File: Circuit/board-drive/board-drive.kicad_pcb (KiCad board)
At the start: 2 copper layers, 164.4 x 98.3 mm, 32 parts, among them M3 MountingHole_3.2mm_M3, P1 XT30, P10 XT60, P2 XT30, P3 XT30, P4 XT30, P5 XT30, P6 XT30, P7 XT30, P8 XT30, P9 XT60, U1 Pololu_Maestro12, U10 PowerDist_WiretoBoard, U11 PowerDist_WiretoBoard, U16 PowerDist_WiretoBoard, U17 PowerDist_WiretoBoard, U18 PowerDist_WiretoBoard, U19 PowerDist_WiretoBoard, U2 Si8660BA-B-IS1, U3 Si8660BA-B-IS1, U8 PowerDist_WiretoBoard, U9 PowerDist_WiretoBoard

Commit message: edited pcb
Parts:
- moved U1 27.8 mm to (52.9, 140.5), turned to 90 degrees
- moved U3 12.4 mm to (78.7, 129.2), turned to 0 degrees
- moved U2 7.31 mm to (65.2, 129.2), turned to 0 degrees
- moved Board Drive 0 6.84 mm to (150.1, 118.6)
- moved Board Drive 1 6.84 mm to (208.6, 119.1)
- moved Board Drive 6 6.84 mm to (208.5, 118.6)
- moved Board Drive 7 6.84 mm to (150.2, 119.1)
- moved Board Drive 2 6.84 mm to (89.9, 118.6)
- moved Board Drive 5 6.84 mm to (89.9, 119.0)
- moved Board Drive 3 6.84 mm to (148.3, 119.0)
- moved Board Drive 4 6.84 mm to (148.3, 118.6)
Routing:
- net GNDA: track 37.7 -> 4.89 mm, vias 2 -> 0
- net /signal0: track 108.7 -> 127.2 mm, vias 1 -> 0
- net /signal1: track 136.2 -> 153.9 mm
- net /signal7: track 24.2 -> 41.6 mm
- net /signal3: track 75.3 -> 90.5 mm, vias 3 -> 1
- net /signal2: track 58.5 -> 44.0 mm, vias 1 -> 0
- net GNDD: track 17.9 -> 4.23 mm
- net /BATTIN_0: track 182.7 -> 174.4 mm
- net /BATTIN_1: track 234.3 -> 241.3 mm
- net /signal8: track 132.6 -> 138.2 mm, vias 0 -> 3
- net /+5v_BEC: track 38.3 -> 43.7 mm
- net /signal6: track 73.5 -> 77.7 mm, vias 0 -> 3
- net /signal9: track 93.8 -> 92.1 mm

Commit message: edited pcb
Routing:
- net /signal2: track 44.0 -> 46.4 mm, vias 0 -> 1
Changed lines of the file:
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@@
   (general
     (links 81)
-    (no_connects 0)
-    (area 43.017657 50.474599 226.07515 197.434901)
+    (no_connects 3)
+    (area 43.017657 50.474599 226.07515 152.2934)
     (thickness 1.6)
     (drawings 38)
-    (tracks 269)
+    (tracks 270)
     (zones 0)
     (modules 32)
@@
   )
   (setup
-    (last_trace_width 2.3622)
+    (last_trace_width 0.254)
     (user_trace_width 0.254)
     (user_trace_width 0.381)
@@
   (segment (start 63.326651 132.163471) (end 63.326651 131.856737) (width 0.1524) (layer B.Cu) (net 17))
   (segment (start 63.326651 131.856737) (end 63.326651 132.331737) (width 0.254) (layer B.Cu) (net 17))
-  (segment (start 67.1322 128.4478) (end 65.6844 129.8956) (width 0.254) (layer F.Cu) (net 18))
+  (segment (start 65.7606 129.9464) (end 64.596651 131.110349) (width 0.254) (layer B.Cu) (net 18))
+  (segment (start 64.596651 131.110349) (end 64.596651 131.856737) (width 0.254) (layer B.Cu) (net 18))
+  (via (at 65.7606 129.9464) (size 0.6) (drill 0.381) (layers F.Cu B.Cu) (net 18))
+  (segment (start 67.2084 128.4986) (end 65.7606 129.9464) (width 0.254) (layer F.Cu) (net 18))
   (segment (start 84.9122 128.4986) (end 67.2084 128.4986) (width 0.254) (layer F.Cu) (net 18))
   (segment (start 87.7316 125.6792) (end 84.9122 128.4986) (width 0.254) (layer F.Cu) (net 18))
@@
   (segment (start 72.507965 131.856737) (end 72.883975 132.232747) (width 0.1524) (layer B.Cu) (net 22))
   (segment (start 69.676651 131.856737) (end 72.507965 131.856737) (width 0.1524) (layer B.Cu) (net 22))
-  (segment (start 58.024975 128.879947) (end 58.101175 128.956147) (width 0.381) (layer B.Cu) (net 23))
-  (segment (start 58.024975 128.879947) (end 58.024975 128.549747) (width 0.254) (layer B.Cu) (net 23))
   (segment (start 69.676651 124.518071) (end 70.978975 123.215747) (width 0.254) (layer B.Cu) (net 23))
   (segment (start 69.676651 126.468737) (end 69.676651 124.518071) (width 0.254) (layer B.Cu) (net 23))
@@
   )
   (zone (net 22) (net_name GNDA) (layer B.Cu) (hatch edge 0.508)
-    (connect_pads (clearance 0.508))
+    (connect_pads yes (clearance 0.508))
     (min_thickness 0.254)
     (fill yes (arc_segments 16) (thermal_gap 0.508) (thermal_bridge_width 0.508))
     (polygon
       (pts
-        (xy 50.9524 130.302) (xy 50.927 130.5052) (xy 50.927 149.606) (xy 214.0458 149.4536) (xy 213.7918 109.8296)
-        (xy 89.8906 110.1598) (xy 89.6366 131.1656) (xy 50.927 130.429)
+        (xy 52.0446 130.556) (xy 51.054 130.556) (xy 51.054 149.86) (xy 214.0458 149.4536) (xy 213.7918 109.8296)
+        (xy 89.8906 110.1598) (xy 89.8906 130.6322) (xy 53.0352 130.556)
       )
     )

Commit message: edited pcb
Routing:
- net /signal0: track 127.2 -> 126.8 mm, vias 0 -> 2
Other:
- board size 164.4 x 98.3 mm -> 164.3 x 98.3 mm
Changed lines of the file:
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@@
     (thickness 1.6)
     (drawings 38)
-    (tracks 270)
+    (tracks 274)
     (zones 0)
     (modules 32)
@@
     (effects (font (size 1.5 1.5) (thickness 0.3)))
   )
-  (gr_line (start 50.0126 51.8414) (end 50 150) (angle 90) (layer Edge.Cuts) (width 0.15))
+  (gr_line (start 50.038 51.8414) (end 50.038 150.114) (angle 90) (layer Edge.Cuts) (width 0.15))
   (gr_line (start 50.038 150.114) (end 214.376 150.114) (angle 90) (layer Edge.Cuts) (width 0.15))
   (gr_line (start 214.3506 51.8414) (end 214.376 150.114) (angle 90) (layer Edge.Cuts) (width 0.15))
-  (gr_line (start 50.0126 51.8414) (end 214.3506 51.8414) (angle 90) (layer Edge.Cuts) (width 0.15))
+  (gr_line (start 50.038 51.8414) (end 214.3506 51.8414) (angle 90) (layer Edge.Cuts) (width 0.15))
   (segment (start 71.52639 65.37961) (end 147.72639 65.37961) (width 1.7272) (layer B.Cu) (net 1))
   (segment (start 147.72639 65.37961) (end 152.654 60.452) (width 1.7272) (layer B.Cu) (net 1))
@@
   (segment (start 69.676651 119.156737) (end 74.280975 123.761061) (width 0.254) (layer F.Cu) (net 24))
   (segment (start 60.786651 126.943737) (end 60.786651 126.468737) (width 0.254) (layer B.Cu) (net 24))
+  (segment (start 62.0522 134.118596) (end 62.0522 131.861188) (width 0.254) (layer B.Cu) (net 25))
+  (segment (start 62.0522 131.861188) (end 62.056651 131.856737) (width 0.254) (layer B.Cu) (net 25))
+  (via (at 62.0522 134.118596) (size 0.6) (drill 0.381) (layers F.Cu B.Cu) (net 25))
+  (segment (start 64.969902 137.036298) (end 62.0522 134.118596) (width 0.254) (layer F.Cu) (net 25))
+  (segment (start 79.0194 136.9822) (end 64.969902 137.036298) (width 0.254) (layer B.Cu) (net 25))
+  (segment (start 65.024 136.9822) (end 64.969902 137.036298) (width 0.254) (layer B.Cu) (net 25))
+  (via (at 64.969902 137.036298) (size 0.6) (drill 0.381) (layers F.Cu B.Cu) (net 25))
   (segment (start 156.4386 112.268) (end 151.4602 112.268) (width 0.254) (layer B.Cu) (net 25))
   (segment (start 151.4602 112.268) (end 148.7424 114.9858) (width 0.254) (layer B.Cu) (net 25))
@@
   (segment (start 148.7424 135.4836) (end 140.6398 143.5862) (width 0.254) (layer B.Cu) (net 25))
   (segment (start 140.6398 143.5862) (end 85.6234 143.5862) (width 0.254) (layer B.Cu) (net 25))
-  (segment (start 79.0194 136.9822) (end 64.008 136.9822) (width 0.254) (layer B.Cu) (net 25))
   (segment (start 85.6234 143.5862) (end 79.0194 136.9822) (width 0.254) (layer B.Cu) (net 25))
-  (segment (start 64.008 136.9822) (end 62.056651 135.030851) (width 0.254) (layer B.Cu) (net 25))
-  (segment (start 62.056651 135.030851) (end 62.056651 131.856737) (width 0.254) (layer B.Cu) (net 25))
   (segment (start 62.056651 132.331737) (end 62.056651 131.856737) (width 0.1524) (layer B.Cu) (net 25))
   (segment (start 62.088975 131.824413) (end 62.056651 131.856737) (width 0.254) (layer B.Cu) (net 25))
@@
     (polygon
       (pts
-        (xy 50.038 79.121) (xy 214.376 79.121) (xy 214.63 109.22) (xy 50.038 109.474)
+        (xy 50.038 79.121) (xy 214.376 79.121) (xy 214.3506 108.8136) (xy 50.038 109.474)
       )
     )

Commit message: edited pcb
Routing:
- net /signal0: track 126.8 -> 131.9 mm, vias 2 -> 3
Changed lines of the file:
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@@
     (thickness 1.6)
     (drawings 38)
-    (tracks 274)
+    (tracks 279)
     (zones 0)
     (modules 32)
@@
   (segment (start 69.676651 119.156737) (end 74.280975 123.761061) (width 0.254) (layer F.Cu) (net 24))
   (segment (start 60.786651 126.943737) (end 60.786651 126.468737) (width 0.254) (layer B.Cu) (net 24))
-  (segment (start 62.0522 134.118596) (end 62.0522 131.861188) (width 0.254) (layer B.Cu) (net 25))
+  (segment (start 60.4012 135.9662) (end 62.056651 134.310749) (width 0.254) (layer B.Cu) (net 25))
+  (segment (start 62.056651 134.310749) (end 62.056651 131.856737) (width 0.254) (layer B.Cu) (net 25))
+  (segment (start 60.4012 141.7066) (end 60.4012 135.9662) (width 0.254) (layer F.Cu) (net 25))
+  (via (at 60.4012 135.9662) (size 0.6) (drill 0.381) (layers F.Cu B.Cu) (net 25))
+  (segment (start 63.6778 144.9832) (end 60.4012 141.7066) (width 0.254) (layer F.Cu) (net 25))
+  (segment (start 134.5946 144.9832) (end 63.6778 144.9832) (width 0.254) (layer F.Cu) (net 25))
+  (segment (start 137.291801 142.285999) (end 134.5946 144.9832) (width 0.254) (layer B.Cu) (net 25))
+  (via (at 134.5946 144.9832) (size 0.6) (drill 0.381) (layers F.Cu B.Cu) (net 25))
+  (segment (start 137.5918 141.986) (end 137.291801 142.285999) (width 0.254) (layer B.Cu) (net 25))
+  (via (at 137.5918 141.986) (size 0.6) (drill 0.381) (layers F.Cu B.Cu) (net 25))
+  (segment (start 141.6812 137.8966) (end 137.5918 141.986) (width 0.254) (layer F.Cu) (net 25))
+  (segment (start 148.844 130.7592) (end 141.7066 137.8966) (width 0.254) (layer F.Cu) (net 25))
+  (segment (start 141.7066 137.8966) (end 141.6812 137.8966) (width 0.254) (layer F.Cu) (net 25))
+  (segment (start 148.844 129.3876) (end 148.844 130.7592) (width 0.254) (layer F.Cu) (net 25))
+  (segment (start 148.844 114.8842) (end 148.844 129.3876) (width 0.254) (layer F.Cu) (net 25))
+  (segment (start 151.4602 112.268) (end 148.844 114.8842) (width 0.254) (layer F.Cu) (net 25))
+  (segment (start 156.4386 112.268) (end 151.4602 112.268) (width 0.254) (layer F.Cu) (net 25))
   (segment (start 62.0522 131.861188) (end 62.056651 131.856737) (width 0.254) (layer B.Cu) (net 25))
-  (via (at 62.0522 134.118596) (size 0.6) (drill 0.381) (layers F.Cu B.Cu) (net 25))
-  (segment (start 64.969902 137.036298) (end 62.0522 134.118596) (width 0.254) (layer F.Cu) (net 25))
-  (segment (start 79.0194 136.9822) (end 64.969902 137.036298) (width 0.254) (layer B.Cu) (net 25))
-  (segment (start 65.024 136.9822) (end 64.969902 137.036298) (width 0.254) (layer B.Cu) (net 25))
-  (via (at 64.969902 137.036298) (size 0.6) (drill 0.381) (layers F.Cu B.Cu) (net 25))
-  (segment (start 156.4386 112.268) (end 151.4602 112.268) (width 0.254) (layer B.Cu) (net 25))
-  (segment (start 151.4602 112.268) (end 148.7424 114.9858) (width 0.254) (layer B.Cu) (net 25))
-  (segment (start 148.7424 114.9858) (end 148.7424 135.4836) (width 0.254) (layer B.Cu) (net 25))
-  (segment (start 148.7424 135.4836) (end 140.6398 143.5862) (width 0.254) (layer B.Cu) (net 25))
-  (segment (start 140.6398 143.5862) (end 85.6234 143.5862) (width 0.254) (layer B.Cu) (net 25))
-  (segment (start 85.6234 143.5862) (end 79.0194 136.9822) (width 0.254) (layer B.Cu) (net 25))
   (segment (start 62.056651 132.331737) (end 62.056651 131.856737) (width 0.1524) (layer B.Cu) (net 25))
   (segment (start 62.088975 131.824413) (end 62.056651 131.856737) (width 0.254) (layer B.Cu) (net 25))

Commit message: edited pcb
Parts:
- added M3: MountingHole_3.2mm_M3, Mounting_Holes:MountingHole_3.2mm_M3, F.Cu at (52.4, 147.3)
- U10, U11, U8, U9: moved to B.Cu
- U16, U17, U18, U19: moved to F.Cu
- moved U8 168.3 mm to (216.4, 66.6), turned to 180 degrees
- moved U16 167.6 mm to (48.9, 66.7), turned to 0 degrees
- moved U9 86.8 mm to (175.7, 66.6), turned to 180 degrees
- moved P8 86.2 mm to (199.2, 60.9), turned to 270 degrees
- moved U17 85.5 mm to (89.6, 66.7), turned to 0 degrees
- moved P1 83.3 mm to (66.5, 60.9), turned to 90 degrees
- moved U19 77.7 mm to (171.1, 66.6), turned to 0 degrees
- moved U11 76.7 mm to (94.2, 66.7), turned to 180 degrees
- moved P6 70.6 mm to (166.8, 60.9), turned to 270 degrees
- moved P3 70.1 mm to (96.9, 61.0), turned to 90 degrees
- moved P5 34.0 mm to (149.5, 60.9)
- moved P4 32.9 mm to (113.7, 61.0)
- moved P7 16.4 mm to (183.2, 60.9)
- moved P2 15.5 mm to (81.4, 61.0)
- moved U10 5.23 mm to (134.9, 66.7), turned to 180 degrees
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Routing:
- net /OUTB_4: track 173.6 -> 21.6 mm
- net /OUTA_5: track 183.1 -> 32.2 mm, vias 1 -> 0
- net /OUTA_4: track 154.8 -> 31.7 mm
- net /OUTB_3: track 22.9 -> 119.3 mm
- net /OUTA_3: track 24.7 -> 102.8 mm
- net /OUTB_0: track 97.6 -> 173.8 mm
- net /OUTB_5: track 93.3 -> 18.1 mm
- net /OUTA_0: track 96.5 -> 163.1 mm
- net /OUTA_1: track 73.9 -> 129.7 mm
- net /OUTB_1: track 72.3 -> 105.8 mm
- net /BATTIN_0: track 174.4 -> 199.5 mm
- net /OUTA_2: track 48.6 -> 28.4 mm
- net /BATTIN_1: track 241.3 -> 222.5 mm
- net /OUTB_7: track 38.9 -> 23.7 mm
- net /OUTA_7: track 38.3 -> 24.3 mm
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
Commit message: edited pcb
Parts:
- U10, U11, U8, U9: moved to F.Cu
- U16, U17, U18, U19: moved to B.Cu
- moved P7 70.1 mm to (113.2, 60.9), turned to 90 degrees
- moved P2 68.1 mm to (149.6, 60.7), turned to 270 degrees
- moved P5 53.1 mm to (96.4, 60.9), turned to 90 degrees
- moved P4 53.1 mm to (166.8, 60.4), turned to 270 degrees
- moved U11 25.0 mm to (69.2, 66.7), turned to 0 degrees
- moved U10 25.0 mm to (109.9, 66.7), turned to 0 degrees
- moved U19 25.0 mm to (196.0, 66.7), turned to 180 degrees
- moved U9 24.9 mm to (150.7, 66.7), turned to 0 degrees
- moved U18 24.9 mm to (155.2, 66.7), turned to 180 degrees
- moved U8 24.9 mm to (191.5, 66.6), turned to 0 degrees
- moved U17 24.9 mm to (114.5, 66.7), turned to 180 degrees
- moved U16 24.8 mm to (73.7, 66.6), turned to 180 degrees
- moved P6 16.6 mm to (183.3, 60.2)
- moved P3 16.0 mm to (80.9, 60.9)
- moved P8 0.79 mm to (199.3, 60.1)
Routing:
- net /OUTB_4: track 21.6 -> 116.4 mm, vias 0 -> 2
- net /OUTA_4: track 31.7 -> 117.0 mm
- net /OUTB_5: track 18.1 -> 81.8 mm
- net /OUTA_3: track 102.8 -> 45.9 mm
- net /OUTA_1: track 129.7 -> 86.0 mm, vias 0 -> 2
- net /OUTA_5: track 32.2 -> 66.3 mm, vias 0 -> 3
- net /OUTA_6: track 33.2 -> 65.7 mm, vias 0 -> 4
- net /OUTB_3: track 119.3 -> 91.3 mm
- net /OUTA_2: track 28.4 -> 52.7 mm, vias 0 -> 2
- net /OUTA_0: track 163.1 -> 140.1 mm
- net /OUTB_6: track 32.0 -> 53.0 mm
- net /BATTIN_1: track 222.5 -> 238.0 mm
- net /BATTIN_0: track 199.5 -> 210.4 mm
- net /OUTB_7: track 23.7 -> 33.2 mm
- net /OUTB_1: track 105.8 -> 97.4 mm, vias 0 -> 2
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
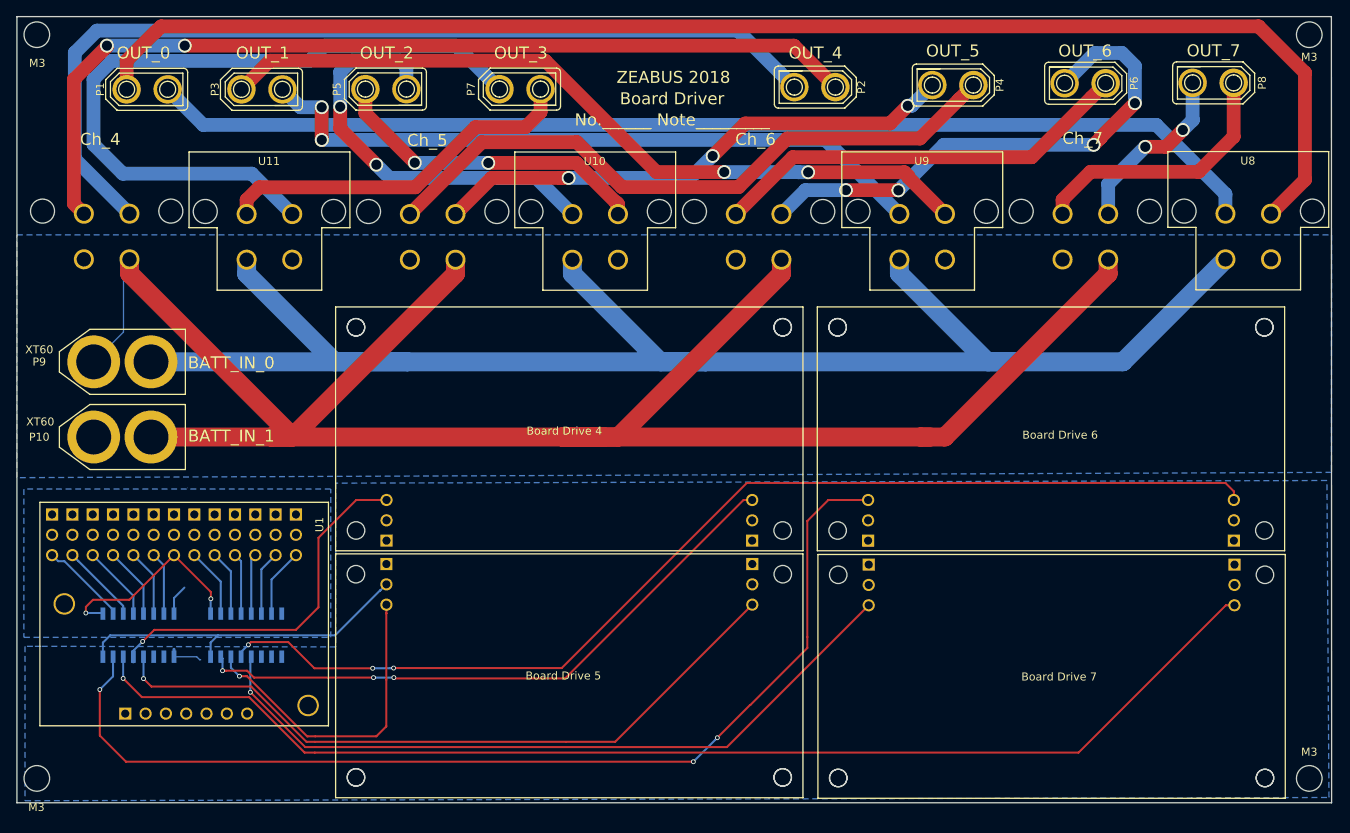
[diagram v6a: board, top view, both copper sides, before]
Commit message: edit trace route and mountring hole
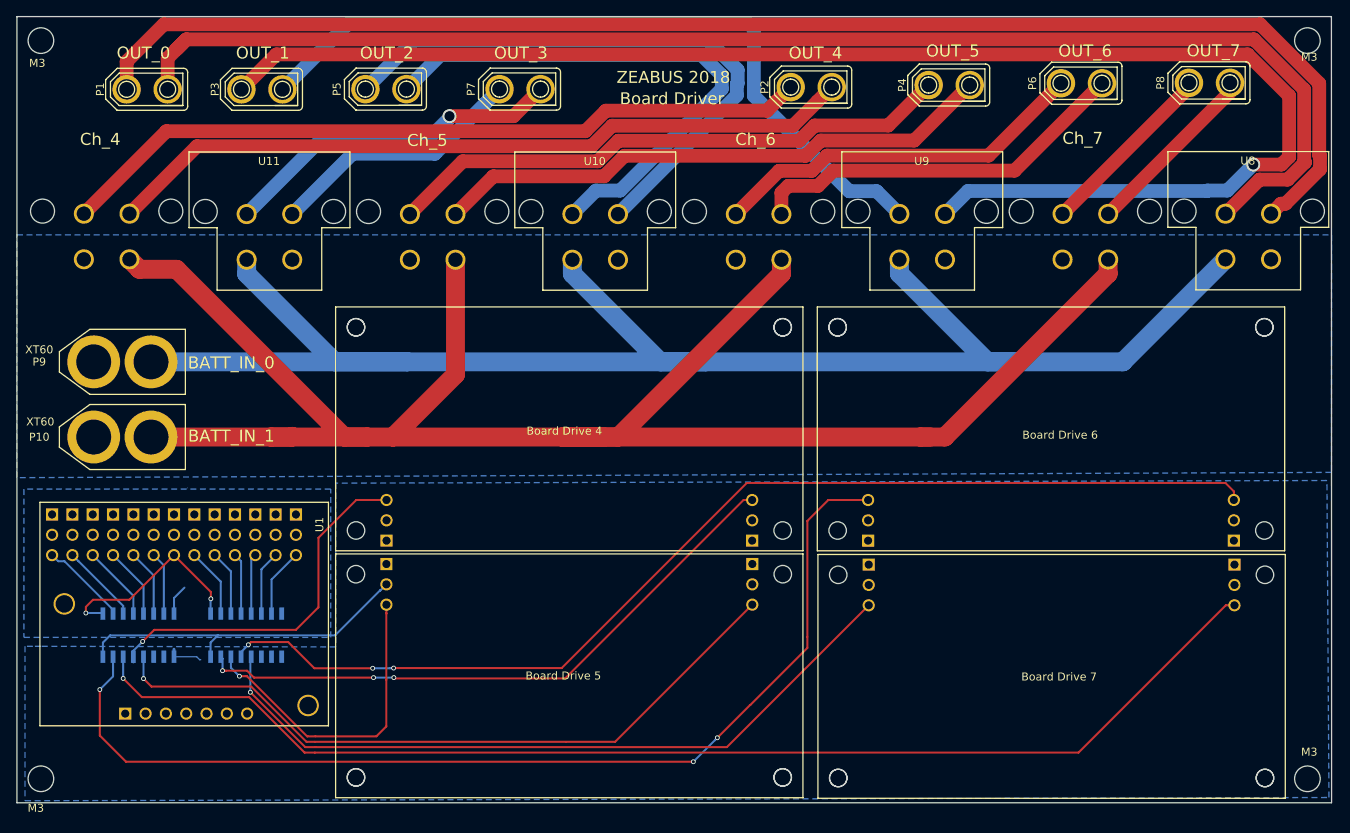
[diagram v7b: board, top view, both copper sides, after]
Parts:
- moved M3 0.13 mm to (52.3, 147.4)
- turned P2 to 90 degrees
- turned P4 to 90 degrees
- turned P6 to 90 degrees
- turned P8 to 90 degrees
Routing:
- net /OUTB_1: track 97.4 -> 188.5 mm, vias 2 -> 1
- net /OUTB_3: track 91.3 -> 32.4 mm
- net /OUTB_2: track 40.6 -> 74.9 mm, vias 2 -> 0
- net /OUTA_0: track 140.1 -> 174.0 mm
- net /OUTA_4: track 117.0 -> 94.3 mm
- net /OUTB_4: track 116.4 -> 94.9 mm, vias 2 -> 0
- net /OUTA_6: track 65.7 -> 48.4 mm, vias 4 -> 0
- net /OUTA_2: track 52.7 -> 69.4 mm, vias 2 -> 0
- net /BATTGND: track 14.4 -> 0.00 mm
- net /OUTB_5: track 81.8 -> 71.5 mm
- net /OUTB_7: track 33.2 -> 22.9 mm
- net /OUTA_1: track 86.0 -> 95.3 mm, vias 2 -> 0
- net /OUTB_6: track 53.0 -> 47.4 mm
- net /OUTA_5: track 66.3 -> 71.0 mm, vias 3 -> 0
- net /BATTIN_1: track 238.0 -> 241.2 mm
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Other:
- board text removed: "No.______ Note_________"

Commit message: fix via near track of signal9, fix OUT3 track and fix zone near zone
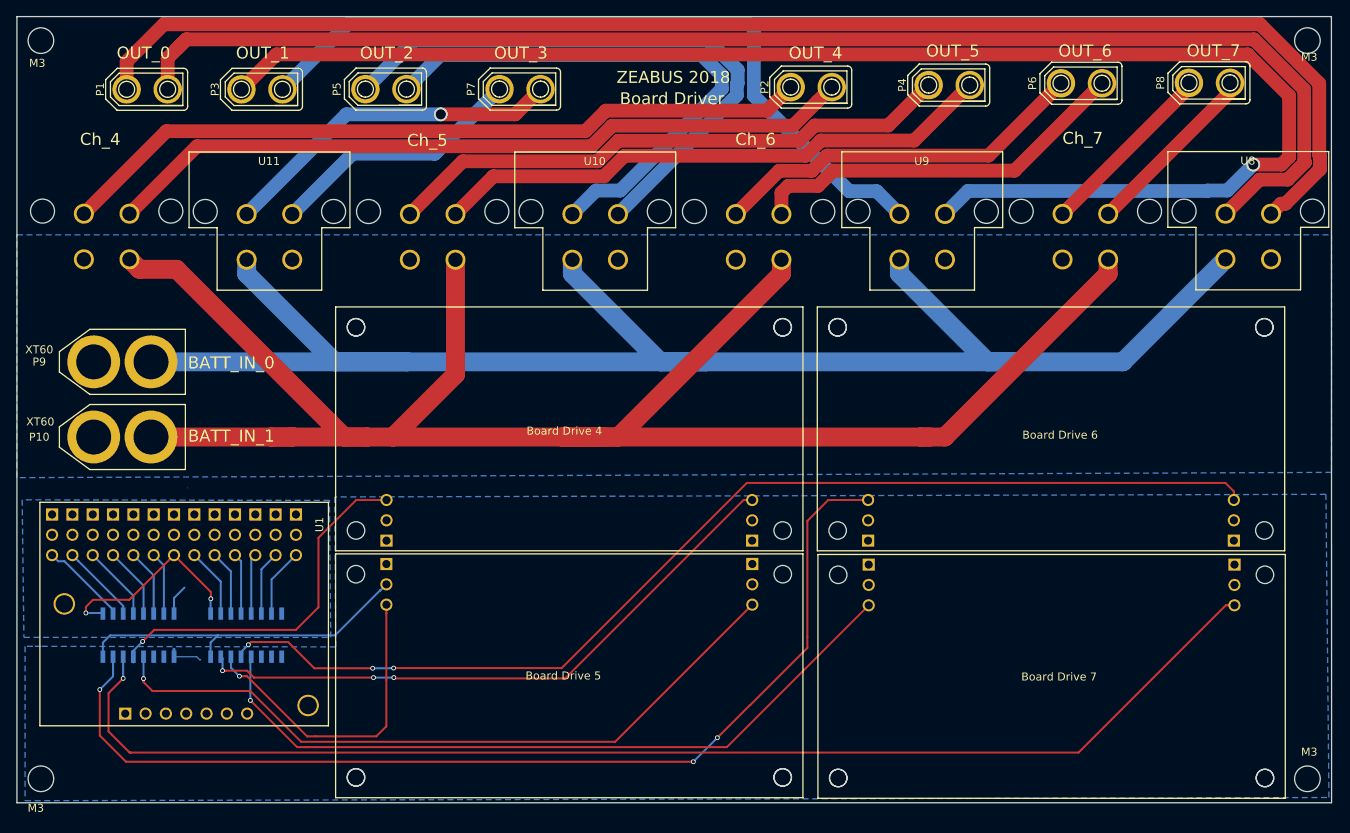
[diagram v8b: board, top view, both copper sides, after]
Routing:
- net /signal1: track 153.9 -> 160.3 mm
- net /signal9: track 92.1 -> 93.0 mm
